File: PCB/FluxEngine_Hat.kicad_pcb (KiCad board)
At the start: 2 copper layers, 83.3 x 24.1 mm, 6 parts, among them J1 CY8CKIT-059 usb & button face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, P1 FDD_IBMPC_host, P2 FDD_SA800_host

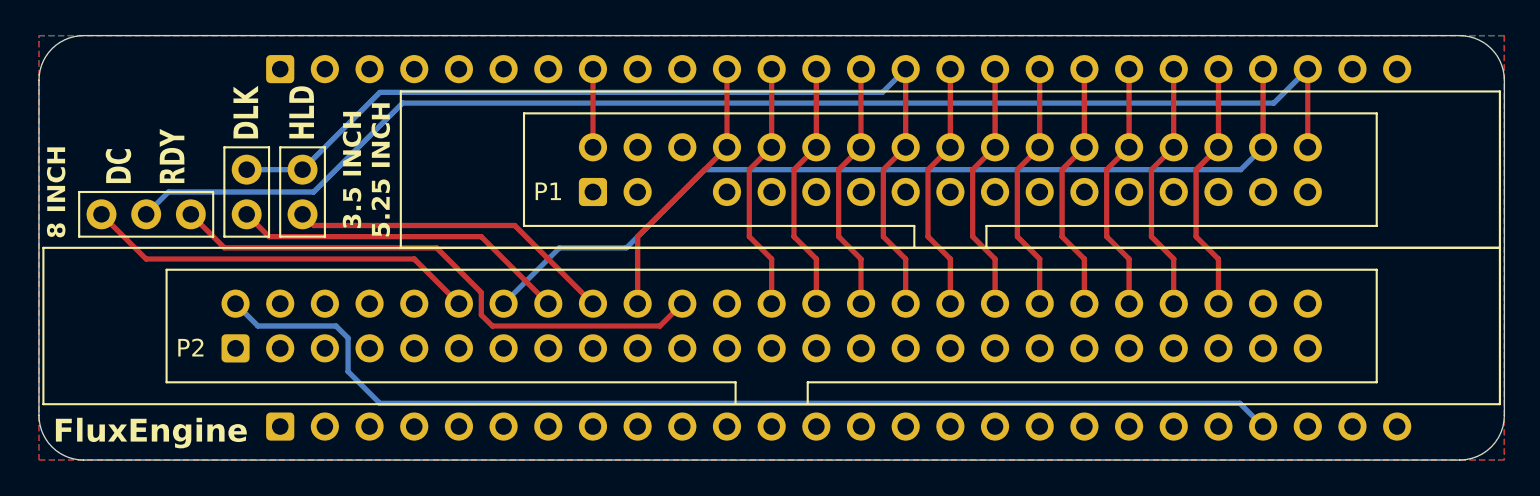
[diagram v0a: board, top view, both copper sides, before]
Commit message: solderless pins footprint, add simple cover for solderless and sockets
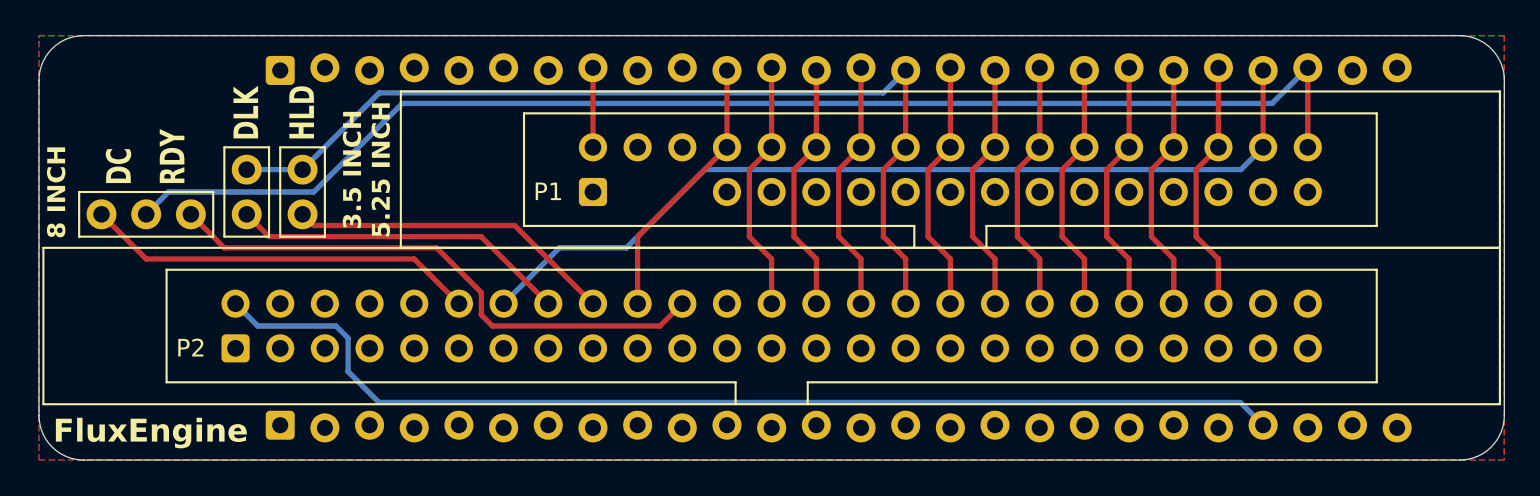
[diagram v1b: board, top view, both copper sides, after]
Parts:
- J1: value CY8CKIT-059 usb & button face away from hat -> CY8CKIT-059; footprint 000_LOCAL:CY8CKIT-059 -> 000_LOCAL:CY8CKIT-059 dry fit
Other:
- board text added: "CY8CKIT-059 usb & button face away from hat"

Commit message: add CDC9406 type 1 & 2
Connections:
- J1 pad J1_12: /~{SEL1} -> /~{MOTB}
- J1 pad J1_13: /~{SEL2} -> /~{DSA}
- J1 pad J1_14: /~{SEL3} -> /~{DSB}
- J1 pad J1_15: /~{SEL4} -> /~{MOTA}
- JP2 pad 2: /~{SEL4} -> /~{MOTA}
- JP3 pad 2: /~{SEL4} -> /~{MOTA}
- P1 pad 10: /~{SEL1} -> /~{MOTB}
- P1 pad 12: /~{SEL2} -> /~{DSA}
- P1 pad 14: /~{SEL3} -> /~{DSB}
- P1 pad 16: /~{SEL4} -> /~{MOTA}
- P2 pad 26: /~{SEL1} -> /~{DSA}
- P2 pad 28: /~{SEL2} -> unconnected-(P2-~{DS2}-Pad28)
- P2 pad 30: /~{SEL3} -> unconnected-(P2-~{DS3}-Pad30)
- P2 pad 32: /~{SEL4} -> unconnected-(P2-~{DS4}-Pad32)
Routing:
- net /~{SEL4}: track 54.1 -> 0.00 mm
- net /~{MOTA}: track 0.00 -> 44.2 mm
- net /~{SEL1}: track 14.5 -> 0.00 mm
- net /~{SEL3}: track 14.5 -> 0.00 mm
- net /~{SEL2}: track 14.3 -> 0.00 mm
- net /~{DSA}: track 0.00 -> 14.3 mm
- net /~{DSB}: track 0.00 -> 4.52 mm
- net /~{MOTB}: track 0.00 -> 4.52 mm
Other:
- board text added: "34pin: IBMPC"
- board text added: "50pin: SA800"
- board text added: "github.com bkw777/FluxEngine_Kit"
- board text added: "v${REVISION}"
- board text removed: "${COMMENT1} v${REVISION}"

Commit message: CDC pinouts
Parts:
- P1: value FDD_IBMPC_host -> FDC_BUS_IBMPC
- P2: value FDD_SA800_host -> FDC_BUS_SA851
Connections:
- J1 pad J1_12: /~{MOTB} -> /~{MOTA}
- J1 pad J1_13: /~{DSA} -> /~{DSB}
- J1 pad J1_14: /~{DSB} -> /~{DSA}
- J1 pad J1_15: /~{MOTA} -> /~{MOTB}
- JP2 pad 2: /~{MOTA} -> /~{MOTB}
- JP3 pad 2: /~{MOTA} -> /~{MOTB}
- P1 pad 10: /~{MOTB} -> /~{MOTA}
- P1 pad 12: /~{DSA} -> /~{DSB}
- P1 pad 14: /~{DSB} -> /~{DSA}
- P1 pad 16: /~{MOTA} -> /~{MOTB}
- P2 pad 26: /~{DSA} -> /~{DSB}
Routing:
- net /~{MOTB}: track 4.52 -> 44.2 mm
- net /~{MOTA}: track 44.2 -> 4.52 mm
- net /~{DSB}: track 4.52 -> 14.3 mm
- net /~{DSA}: track 14.3 -> 4.52 mm
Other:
- board text added: "50pin: SA850"
- board text removed: "50pin: SA800"

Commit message: silkscreen, pics
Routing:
- net /SIDE: track 51.2 -> 53.5 mm
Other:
- board text added: "34-pin: IBMPC"
- board text added: "50-pin: Shugart"
- board text added: "DSKCHG"
- board text added: "INUSE"
- board text added: "READY"
- board text added: "Shugart"
- board text removed: "34pin: IBMPC"
- board text removed: "50pin: SA850"
- board text removed: "DC"
- board text removed: "DLK"
- board text removed: "FluxEngine"
- board text removed: "RDY"

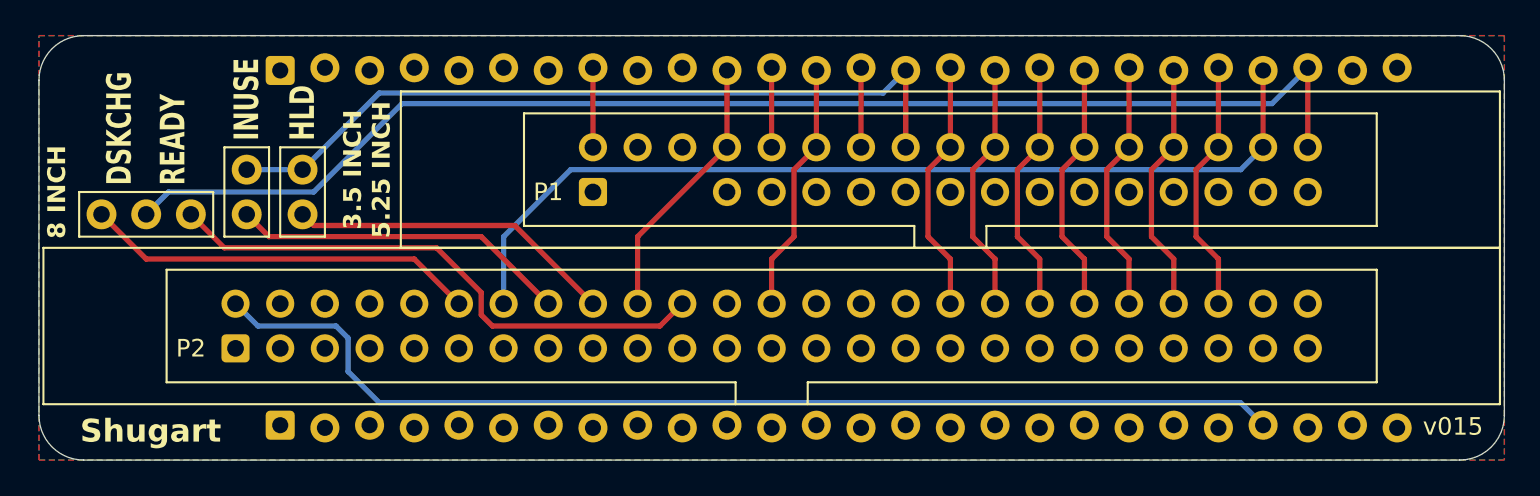
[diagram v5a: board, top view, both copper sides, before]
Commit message: reduce thermal spoke width
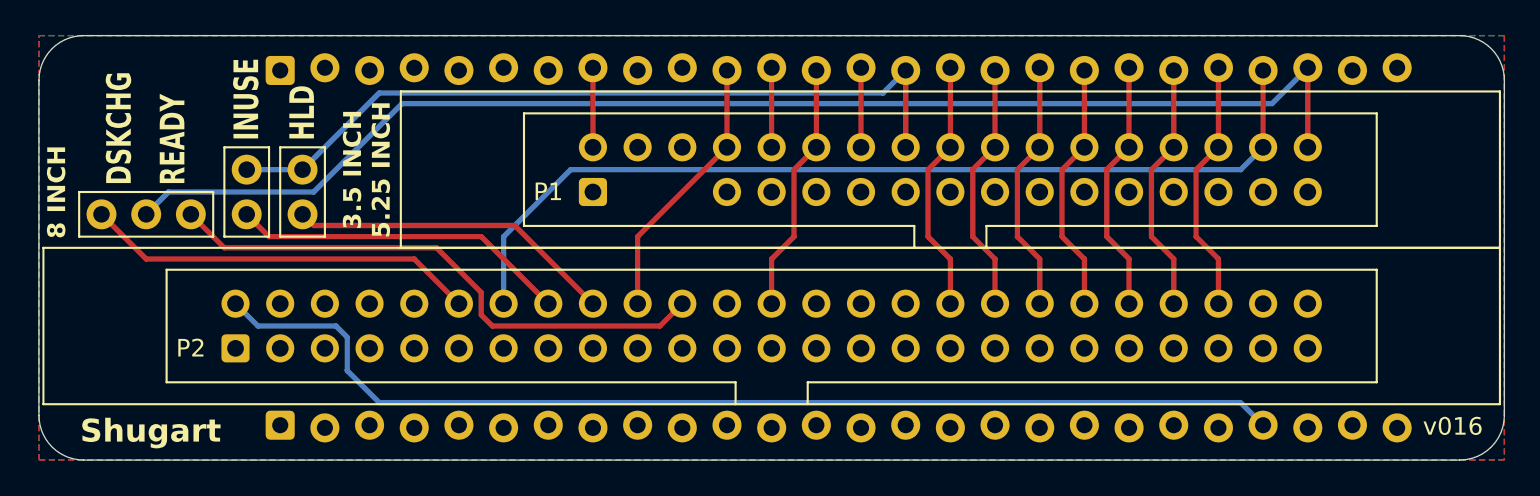
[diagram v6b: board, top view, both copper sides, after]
